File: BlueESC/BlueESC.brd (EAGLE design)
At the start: 24.4 x 36 mm, 46 parts, among them Q1 BC817-40W, Q2 BC817-40W, Q3 BC817-40W, Q4 SI7370, Q5 SI7370, Q6 SI7370, Q7 SI7370, Q8 SI7370, Q9 SI7370

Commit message: Combined logic and power boards into a single board. This is done for several reasons. The first is to create a consistent single schematic to help others view the design. The second is for manufacturing and avoiding double cost of setup.
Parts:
- added C4, C5, C7: 0.1uF, SparkFun-Capacitors:0603-CAP
- added C6: 1uF, SparkFun-Capacitors:0603-CAP
- added C9: 1uF, SparkFun-Capacitors:EIA3216
- added LED1: BLUE, BR-Eagle-Library:SMT-LED-3X2-RA
- added LED2: RED, BR-Eagle-Library:SMT-LED-3X2-RA
- added LOGO1: OSHW-LOGOS, SparkFun-Aesthetics:OSHW-LOGO-S
- added R1, R2, R3, R4, R5, R6: 47K, SparkFun-Resistors:0603-RES
- added R10: 18K 1%, SparkFun-Resistors:0603-RES
- added R11: 3.3K 1%, SparkFun-Resistors:0603-RES
- added R12, R13, R14: 10K, SparkFun-Resistors:0603-RES
- added R15: 1K, SparkFun:0603-RES
- added R16: 4.7K, SparkFun:0603-RES
- added R34: 47K, SparkFun:0603-RES
- added R35: 470K, SparkFun:0603-RES
- added R7, R8, R9: 4.7K, SparkFun-Resistors:0603-RES
- added U$10: LOGOBR-LOGO-M, BR-Eagle-Library:BR-LOGO-MEDIUM
- added U$11, U$12, U$13, U$14: PAD1.5X3MM, BR-Eagle-Library:PAD-1.5X3MM
- added U$16: HEADER-62MM, BR-Eagle-Library:HEADER-2MM-6POS
- added U$17: HEADER-122MM, BR-Eagle-Library:HEADER-2MM-12POS
- added U1: ATMEGA168, SparkFun-DigitalIC:TQFP32-08
- added U2: V_REG_LDOSMD, SparkFun-PowerIC:SOT23-5
- added Y1: RESONATORSMD, SparkFun:RESONATOR-SMD
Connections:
- new net CENTER: R1.1, R2.1, R3.1, U1.10
- new net CURRENT_ADC_FILTERED: C6.1, R34.2, U1.26
- new net LED_STATUS: LED1.2, U1.14
- new net LED_WARN: R16.2, U1.13
- new net L_CURRENT_ADC: R34.1, U$17.P$4
- new net L_GND: C4.2, C5.2, C6.2, C7.2, C9.C, LED2.2, R11.1, R35.1, R7.1, R8.1, R9.1, U$11.P$1, U$16.P$1, U$17.P$1, U$17.P$12, U$17.P$2, U1.21, U1.3, U1.5, U2.2, Y1.2
- new net L_PHASE_A: R4.2, U$16.P$2
- new net L_PHASE_B: R5.2, U$16.P$3
- new net L_PHASE_C: R6.2, U$16.P$4
- new net L_PWM_AH: U$17.P$5, U1.32
- new net L_PWM_AL: U$17.P$6, U1.1
- new net L_PWM_BH: U$17.P$7, U1.2
- new net L_PWM_BL: U$17.P$8, U1.9
- new net L_PWM_CH: U$17.P$9, U1.11
- new net L_PWM_CL: U$17.P$10, U1.15
- new net L_TEMP_ADC: U$16.P$5, U1.22
- new net L_VBAT: R10.2, U$17.P$11, U2.1
- new net MISO: U1.16
- new net N$10: U1.7, Y1.1
- new net N$11: U1.8, Y1.3
- new net N$16: LED1.1, R15.1
- new net N$3: LED2.1, R16.1
- new net PWM: R35.2, U$14.P$1, U1.12
- new net RESET: C5.1, R12.1, U1.29
- new net RX: U1.30
- new net SCK: U1.17
- new net SCL: R14.1, U$13.P$1, U1.28
- new net SDA: R13.1, U$12.P$1, U1.27
- new net SENSE_A: R1.2, R4.1, R7.2, U1.23
- new net SENSE_B: R2.2, R5.1, R8.2, U1.24
- new net SENSE_C: R3.2, R6.1, R9.2, U1.25
- new net TX: U1.31
- new net VBAT_ADC: R10.1, R11.2, U1.19
- new net VCC5V: C4.1, C7.1, C9.A, R12.2, R13.2, R14.2, R15.2, U$16.P$6, U$17.P$3, U1.18, U1.20, U1.4, U1.6, U2.5
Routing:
- net VCC5V: track 0.00 -> 87.6 mm, vias 0 -> 6
- net CENTER: track 0.00 -> 33.0 mm, vias 0 -> 2
- net SENSE_C: track 0.00 -> 27.7 mm, vias 0 -> 2
- net LED_WARN: track 0.00 -> 23.8 mm, vias 0 -> 2
- net LED_STATUS: track 0.00 -> 21.7 mm, vias 0 -> 2
- net L_VBAT: track 0.00 -> 21.2 mm, vias 0 -> 2
- net RESET: track 0.00 -> 20.5 mm, vias 0 -> 2
- net PWM: track 0.00 -> 18.7 mm, vias 0 -> 2
- net VBAT_ADC: track 0.00 -> 18.5 mm, vias 0 -> 2
- net SENSE_B: track 0.00 -> 18.1 mm, vias 0 -> 2
- net L_GND: track 0.00 -> 15.4 mm, vias 0 -> 8
- net SCL: track 0.00 -> 14.6 mm
- net L_PWM_CL: track 0.00 -> 12.1 mm, vias 0 -> 1
- net CURRENT_ADC_FILTERED: track 0.00 -> 12.1 mm, vias 0 -> 2
- net L_TEMP_ADC: track 0.00 -> 12.0 mm, vias 0 -> 1
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- added copper zone on layer 1, net L_GND
- added copper zone on layer 16, net L_GND
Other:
- board size 24.4 x 36 mm -> 50 x 36 mm
- board text added: "9/15"
- board text added: "BLK"
- board text added: "BLUEESC-ELEC-LOGIC"
- board text added: "BlueESC"
- board text added: "BlueRobotics"
- board text added: "Designed by R. Jehangir"
- board text added: "GRN"
- board text added: "PWM"
- board text added: "R"
- board text added: "R/Y"
- board text added: "SCL"
- board text added: "SDA"
- board text added: "WHT"
- board text added: "rev8"
- board text removed: "rev5"

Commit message: Put R20 on back of power board to minimize soldering errors.
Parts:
- flipped R20 to the bottom
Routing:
- net PHASE_C: track 22.5 -> 18.2 mm
- net TEMP_ADC: track 18.3 -> 18.9 mm, vias 1 -> 2
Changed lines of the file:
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@@
 <element name="R18" library="SparkFun-Resistors" package="0603-RES" value="4.7K" x="19.4818" y="8.4074" rot="R180"/>
 <element name="R19" library="SparkFun-Resistors" package="0603-RES" value="100" x="15.6718" y="8.4074" rot="R180"/>
-<element name="R20" library="SparkFun-Resistors" package="0603-RES" value="3.3K 1%" x="1.54305" y="26.34615" rot="R270"/>
+<element name="R20" library="SparkFun-Resistors" package="0603-RES" value="3.3K 1%" x="1.54305" y="26.34615" rot="MR270"/>
 <element name="R21" library="SparkFun-Resistors" package="0603-RES" value="100" x="19.4818" y="12.2174" rot="R180"/>
 <element name="R22" library="SparkFun-Resistors" package="0603-RES" value="10K" x="15.6718" y="12.5349" rot="R180"/>
@@
 <wire x1="11.06805" y1="30.3149" x2="11.06805" y2="29.6799" width="0.3048" layer="16"/>
 <wire x1="11.06805" y1="29.6799" x2="12.8143" y2="29.6799" width="0.3048" layer="16"/>
-<wire x1="1.9304" y1="29.6164" x2="3.9243" y2="25.8699" width="0.3048" layer="16"/>
 <wire x1="3.9243" y1="25.8699" x2="2.3368" y2="24.44115" width="0.3048" layer="16"/>
 <wire x1="2.3368" y1="24.44115" x2="2.3368" y2="20.28115" width="0.3048" layer="16"/>
@@
 <wire x1="2.3368" y1="24.12365" x2="2.3368" y2="22.1224" width="0.3048" layer="1"/>
 <wire x1="2.3368" y1="22.1224" x2="1.0668" y2="20.8524" width="0.3048" layer="1"/>
-<wire x1="1.54305" y1="27.19615" x2="1.96305" y2="27.19615" width="0.3048" layer="1"/>
-<wire x1="1.96305" y1="27.19615" x2="2.49555" y2="26.66365" width="0.3048" layer="1"/>
-<wire x1="2.49555" y1="26.66365" x2="2.49555" y2="25.2349" width="0.3048" layer="1"/>
-<wire x1="2.49555" y1="25.2349" x2="2.9718" y2="24.75865" width="0.3048" layer="1"/>
+<wire x1="1.54305" y1="27.19615" x2="2.96635" y2="27.19615" width="0.3048" layer="16"/>
+<wire x1="2.96635" y1="27.19615" x2="3.01625" y2="27.14625" width="0.3048" layer="16"/>
+<via x="3.01625" y="27.14625" extent="1-16" drill="0.5"/>
+<wire x1="3.01625" y1="27.14625" x2="3.01625" y2="24.8031" width="0.3048" layer="1"/>
+<wire x1="3.01625" y1="24.8031" x2="2.9718" y2="24.75865" width="0.3048" layer="1"/>
 </signal>
 <signal name="PWM_CH">
@@
 <contactref element="U$4" pad="P$6"/>
 <contactref element="R20" pad="2"/>
-<wire x1="1.54305" y1="25.49615" x2="1.54305" y2="23.32865" width="0.3048" layer="1"/>
-<wire x1="1.54305" y1="23.32865" x2="1.0668" y2="22.8524" width="0.254" layer="1"/>
+<wire x1="1.0668" y1="22.8524" x2="1.0668" y2="22.9743" width="0.3048" layer="16"/>
+<wire x1="1.0668" y1="22.9743" x2="1.5875" y2="23.495" width="0.3048" layer="16"/>
+<wire x1="1.5875" y1="23.495" x2="1.5875" y2="25.4517" width="0.3048" layer="16"/>
+<wire x1="1.5875" y1="25.4517" x2="1.54305" y2="25.49615" width="0.3048" layer="16"/>
 </signal>
 <signal name="VCC5V-2">

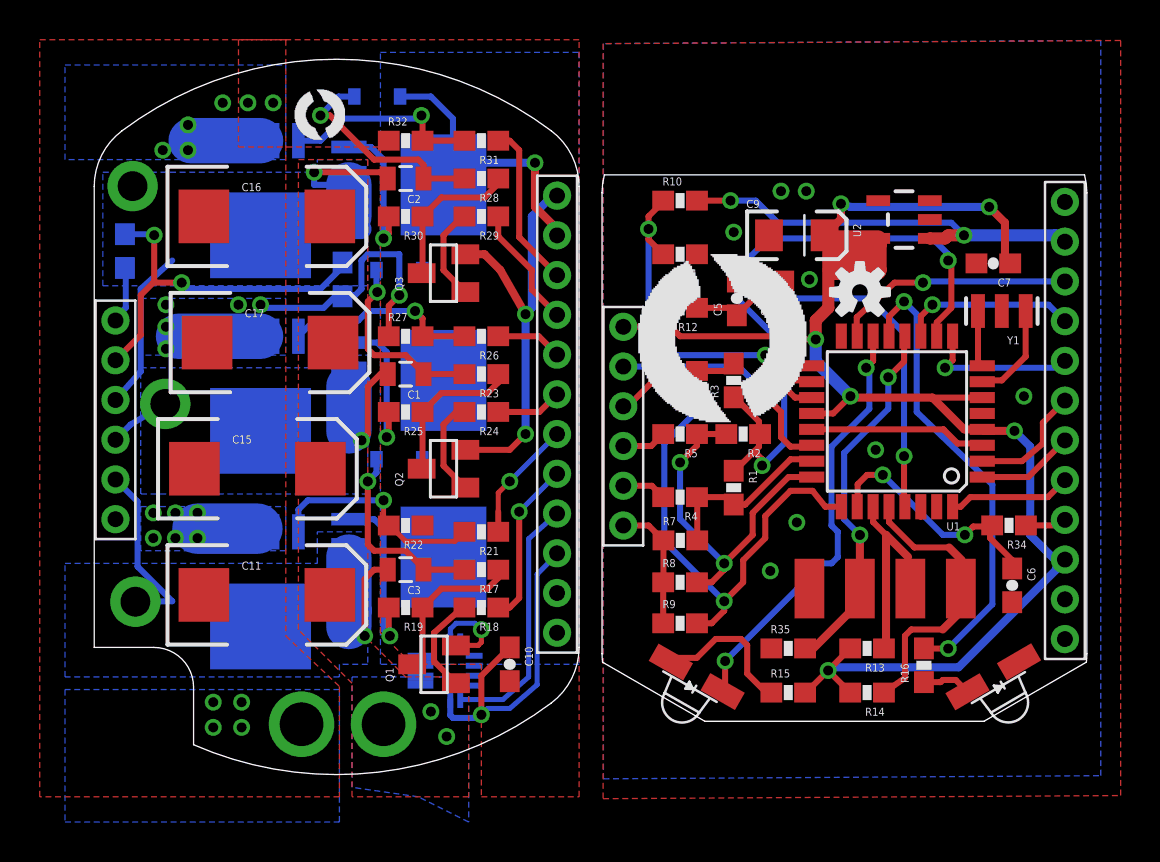
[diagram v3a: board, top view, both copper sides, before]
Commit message: Updated MOSFET footprint to TDSON-8 to accommodate new FET and to fix potential soldering errors. This should still fit the SiR158DP as well.
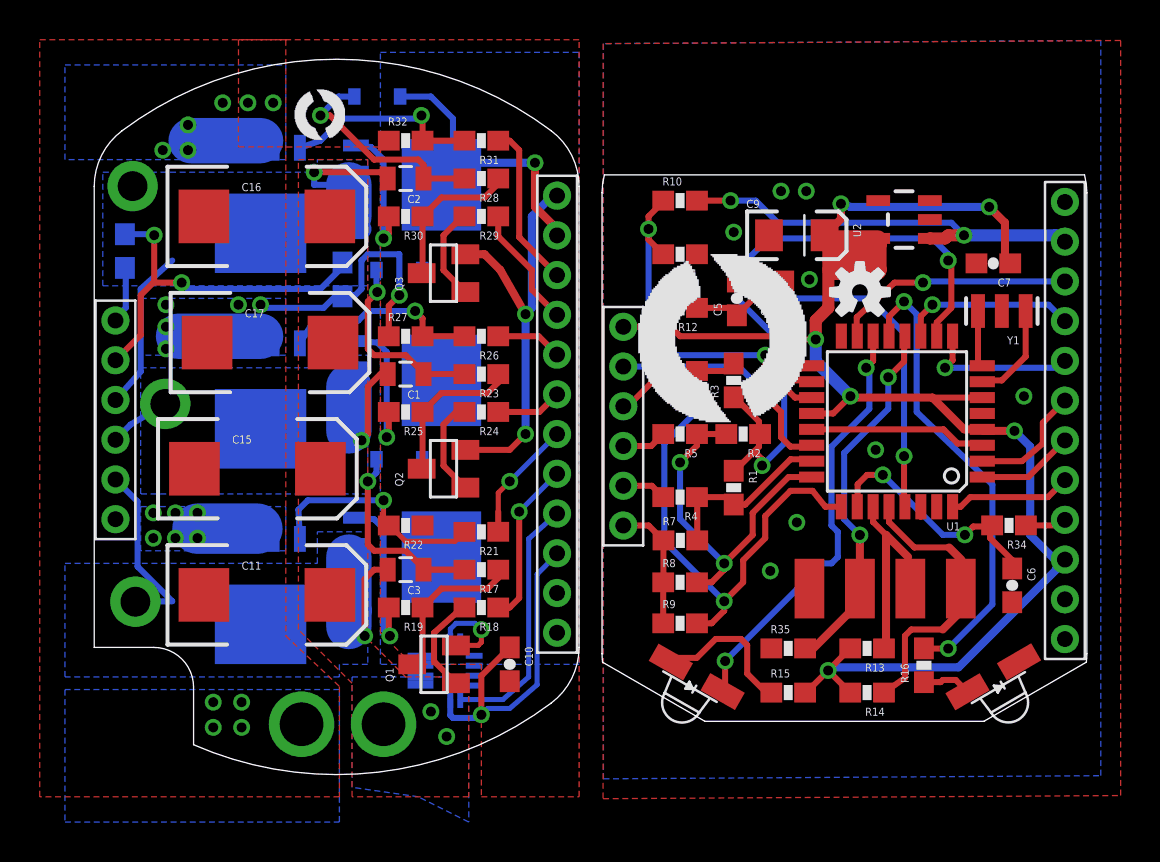
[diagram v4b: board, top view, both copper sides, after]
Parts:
- C1, C2, C3: value 1uF -> 1uF 60V
- Q4, Q5, Q6, Q7, Q8, Q9: value SI7370 -> MOSFET-NCHANNEL; device transistor-fet-bobstarr:POWERPAK-SO-08 -> BlueRobotics-Main:TDSON-8
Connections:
- net GATE_AH: now also Q4.G; no longer Q4.4
- net GATE_AL: now also Q5.G; no longer Q5.4
- net GATE_BH: now also Q6.G; no longer Q6.4
- net GATE_BL: now also Q7.G; no longer Q7.4
- net GATE_CH: now also Q8.G; no longer Q8.4
- net GATE_CL: now also Q9.G; no longer Q9.4
- net GND: now also Q5.S1, Q5.S2, Q5.S3, Q7.S1, Q7.S2, Q7.S3, Q9.S1, Q9.S2, Q9.S3; no longer Q5.3, Q7.3, Q9.3
- net PHASE_A: now also Q4.S1, Q4.S2, Q4.S3, Q5.D; no longer Q4.3, Q5.5-8
- net PHASE_B: now also Q6.S1, Q6.S2, Q6.S3, Q7.D; no longer Q6.3, Q7.5-8
- net PHASE_C: now also Q8.S1, Q8.S2, Q8.S3, Q9.D; no longer Q8.3, Q9.5-8
- net VBAT: now also Q4.D, Q6.D, Q8.D; no longer Q4.5-8, Q6.5-8, Q8.5-8
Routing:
- net GND: track 50.2 -> 51.2 mm

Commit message: Minor updates and reference marking for Vscore.
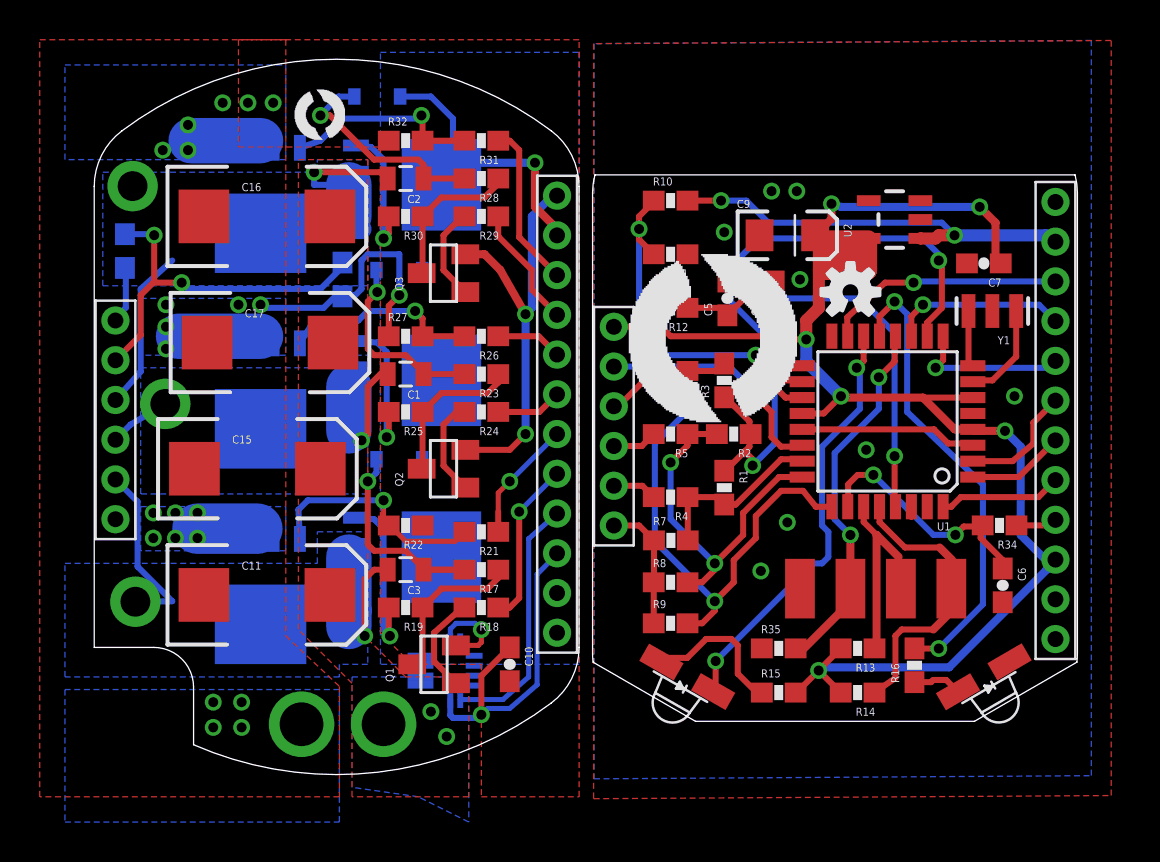
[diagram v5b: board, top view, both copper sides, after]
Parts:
- moved R1 0.48 mm to (31.7, 14.4)
- moved R3 0.48 mm to (31.7, 19.8)
- moved C4 0.48 mm to (34.2, 24.0)
- moved C5 0.48 mm to (31.9, 24.0)
- moved C6 0.48 mm to (45.7, 9.53)
- moved C7 0.48 mm to (44.8, 25.7)
- moved C9 0.48 mm to (34.9, 27.1)
- moved LED1 0.48 mm to (29.8, 4.92)
- moved LED2 0.48 mm to (44.8, 4.92)
- moved LOGO1 0.48 mm to (38.1, 24.3)
- moved R10 0.48 mm to (29.0, 28.9)
- moved R11 0.48 mm to (29.0, 26.2)
- moved R12 0.48 mm to (29.0, 23.5)
- moved R13 0.48 mm to (38.4, 6.35)
- moved R14 0.48 mm to (38.4, 4.13)
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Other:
- board size 50 x 36 mm -> 49.5 x 36 mm
- board text added: "VSCORE"

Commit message: Removed a ground via that was too close to a solder point.
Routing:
- net GND: vias 25 -> 24
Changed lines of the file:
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@@
 <via x="8.3693" y="23.6474" extent="1-16" drill="0.5"/>
 <via x="7.25805" y="23.6474" extent="1-16" drill="0.5"/>
-<via x="3.44805" y="31.42615" extent="1-16" drill="0.5"/>
 <via x="4.71805" y="31.42615" extent="1-16" drill="0.5"/>
 <via x="9.0043" y="33.8074" extent="1-16" drill="0.5"/>
